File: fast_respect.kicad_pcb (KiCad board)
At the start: 2 copper layers, 70 x 110 mm, 97 parts, among them J1_1 Conn_02x04_Odd_Even, J5_1 Conn_02x03_Odd_Even, J5_2 Conn_02x03_Odd_Even, J7_1 Conn_01x02, Q2_1 IRLML6402, Q3_1 IRLML6344T, Q4_1 IRLML6344T, Q4_2 IRLML6344T, Q4_3 IRLML6344T, Q4_4 IRLML6344T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

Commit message: DRV8835のフットプリントをネットリストに反映させてPCBも更新した
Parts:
- U5_1: footprint Self-Made_Generic_Packages:WSON-12-1EP_ExpandPad_3x2mm_P0.5mm_EP1x2.65 -> DRV8835:DRV8835_ThermalExpanded_WSON-12-1EP
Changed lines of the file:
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@@
     )
   )
-  (footprint "Self-Made_Generic_Packages:WSON-12-1EP_ExpandPad_3x2mm_P0.5mm_EP1x2.65" (layer "F.Cu")
+  (footprint "DRV8835:DRV8835_ThermalExpanded_WSON-12-1EP" (layer "F.Cu")
     (at -46.435 69.39 90)
     (descr "WSON-12 http://www.ti.com/lit/ds/symlink/lm27762.pdf")
@@
         (effects (font (size 1 1) (thickness 0.15)))
     )
-    (fp_text user "${REFERENCE}" (at 0 -0.25) (layer "F.Fab")
+    (fp_text user "${REFERENCE}" (at 0 -0.25 180) (layer "F.Fab")
         (effects (font (size 0.5 0.5) (thickness 0.05)))
     )
@@
     (pad "6" smd rect (at -1.075 1.25 90) (size 0.75 0.25) (layers "F.Cu" "F.Paste" "F.Mask")
       (net 6 "GND") (pinfunction "GND") (pintype "power_in"))
+    (pad "6" smd rect (at 0 0 90) (size 1 3.975) (layers "F.Cu" "F.Mask")
+      (net 6 "GND") (pinfunction "GND") (pintype "power_in"))
     (pad "7" smd rect (at 1.075 1.25 90) (size 0.75 0.25) (layers "F.Cu" "F.Paste" "F.Mask")
       (net 7 "MOTOR2_PWM") (pinfunction "BIN2/B_ENABLE") (pintype "input"))
@@
     (pad "12" smd rect (at 1.075 -1.25 90) (size 0.75 0.25) (layers "F.Cu" "F.Paste" "F.Mask")
       (net 10 "+3.3V") (pinfunction "VCC") (pintype "power_in"))
-    (pad "13" smd rect (at 0 0 90) (size 1 3.975) (layers "F.Cu" "F.Mask"))
     (model "${KICAD6_3DMODEL_DIR}/Package_SON.3dshapes/WSON-12-1EP_3x2mm_P0.5mm_EP1x2.65.wrl"
       (offset (xyz 0 0 0))

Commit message: 距離センサのPCB位置を考慮してピン割り当てを変更した（1,2,3,4 -> 4,3,2,1）
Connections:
- U1_1 pad 10: DIST_ADC_2 -> DIST_ADC_3
- U1_1 pad 11: DIST_LED_2 -> DIST_LED_3
- U1_1 pad 20: DIST_ADC_3 -> DIST_ADC_2
- U1_1 pad 21: DIST_LED_3 -> DIST_LED_2
- U1_1 pad 22: DIST_ADC_4 -> DIST_ADC_1
- U1_1 pad 23: DIST_LED_4 -> DIST_LED_1
- U1_1 pad 8: DIST_ADC_1 -> DIST_ADC_4
- U1_1 pad 9: DIST_LED_1 -> DIST_LED_4
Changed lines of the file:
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@@
       (net 72 "NRST") (pinfunction "NRST") (pintype "input"))
     (pad "8" smd roundrect (at -5.675 -0.25 225) (size 1.55 0.3) (layers "F.Cu" "F.Paste" "F.Mask") (roundrect_rratio 0.25)
-      (net 38 "DIST_ADC_1") (pinfunction "PC0") (pintype "bidirectional"))
+      (net 35 "DIST_ADC_4") (pinfunction "PC0") (pintype "bidirectional"))
     (pad "9" smd roundrect (at -5.675 0.25 225) (size 1.55 0.3) (layers "F.Cu" "F.Paste" "F.Mask") (roundrect_rratio 0.25)
-      (net 41 "DIST_LED_1") (pinfunction "PC1") (pintype "bidirectional"))
+      (net 53 "DIST_LED_4") (pinfunction "PC1") (pintype "bidirectional"))
     (pad "10" smd roundrect (at -5.675 0.75 225) (size 1.55 0.3) (layers "F.Cu" "F.Paste" "F.Mask") (roundrect_rratio 0.25)
-      (net 37 "DIST_ADC_2") (pinfunction "PC2") (pintype "bidirectional"))
+      (net 36 "DIST_ADC_3") (pinfunction "PC2") (pintype "bidirectional"))
     (pad "11" smd roundrect (at -5.675 1.25 225) (size 1.55 0.3) (layers "F.Cu" "F.Paste" "F.Mask") (roundrect_rratio 0.25)
-      (net 45 "DIST_LED_2") (pinfunction "PC3") (pintype "bidirectional"))
+      (net 49 "DIST_LED_3") (pinfunction "PC3") (pintype "bidirectional"))
     (pad "12" smd roundrect (at -5.675 1.75 225) (size 1.55 0.3) (layers "F.Cu" "F.Paste" "F.Mask") (roundrect_rratio 0.25)
       (net 6 "GND") (pinfunction "VSSA") (pintype "power_in"))
@@
       (net 10 "+3.3V") (pinfunction "VDD") (pintype "power_in"))
     (pad "20" smd roundrect (at -2.25 5.675 225) (size 0.3 1.55) (layers "F.Cu" "F.Paste" "F.Mask") (roundrect_rratio 0.25)
-      (net 36 "DIST_ADC_3") (pinfunction "PA4") (pintype "bidirectional"))
+      (net 37 "DIST_ADC_2") (pinfunction "PA4") (pintype "bidirectional"))
     (pad "21" smd roundrect (at -1.75 5.675 225) (size 0.3 1.55) (layers "F.Cu" "F.Paste" "F.Mask") (roundrect_rratio 0.25)
-      (net 49 "DIST_LED_3") (pinfunction "PA5") (pintype "bidirectional"))
+      (net 45 "DIST_LED_2") (pinfunction "PA5") (pintype "bidirectional"))
     (pad "22" smd roundrect (at -1.25 5.675 225) (size 0.3 1.55) (layers "F.Cu" "F.Paste" "F.Mask") (roundrect_rratio 0.25)
-      (net 35 "DIST_ADC_4") (pinfunction "PA6") (pintype "bidirectional"))
+      (net 38 "DIST_ADC_1") (pinfunction "PA6") (pintype "bidirectional"))
     (pad "23" smd roundrect (at -0.75 5.675 225) (size 0.3 1.55) (layers "F.Cu" "F.Paste" "F.Mask") (roundrect_rratio 0.25)
-      (net 53 "DIST_LED_4") (pinfunction "PA7") (pintype "bidirectional"))
+      (net 41 "DIST_LED_1") (pinfunction "PA7") (pintype "bidirectional"))
     (pad "24" smd roundrect (at -0.25 5.675 225) (size 0.3 1.55) (layers "F.Cu" "F.Paste" "F.Mask") (roundrect_rratio 0.25)
       (net 39 "UI_LED_1") (pinfunction "PC4") (pintype "bidirectional"))

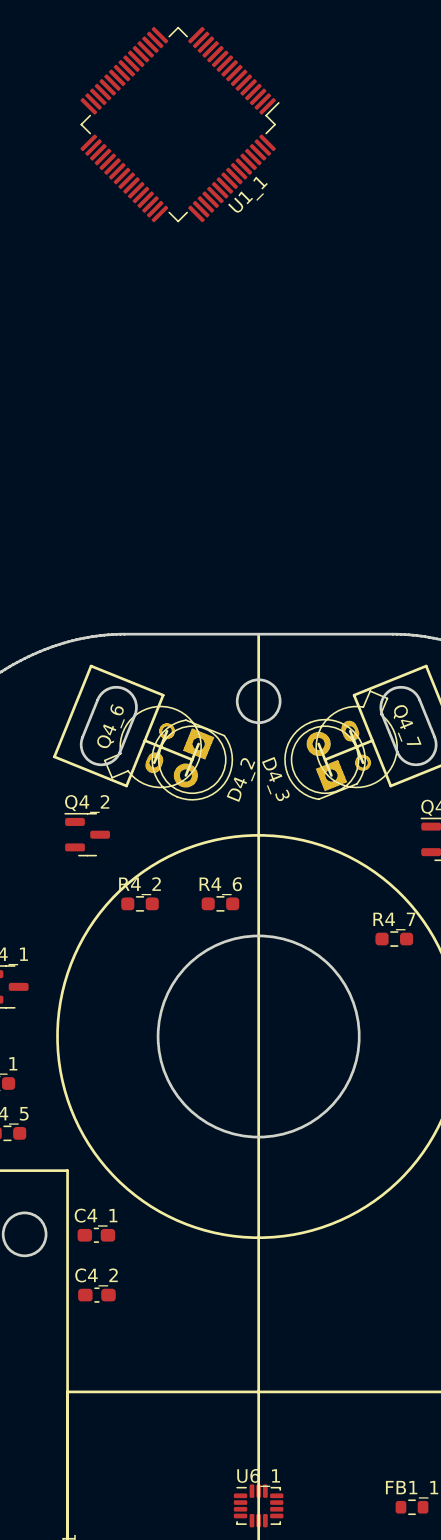
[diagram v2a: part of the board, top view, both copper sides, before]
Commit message: マイコンの位置を再調整
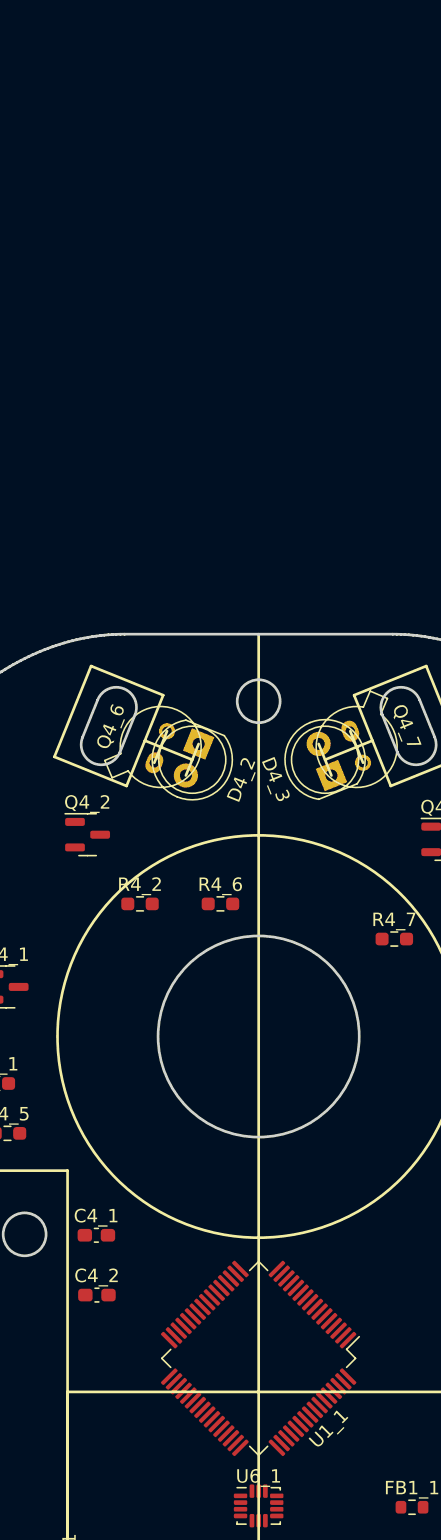
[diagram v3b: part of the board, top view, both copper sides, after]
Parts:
- moved U1_1 92.2 mm to (-35.0, 54.0)
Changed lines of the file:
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@@
   )
   (footprint "Package_QFP:LQFP-64_10x10mm_P0.5mm" (layer "F.Cu")
-    (at -41 -38 -135)
+    (at -35 54 -135)
     (descr "LQFP, 64 Pin (https://www.analog.com/media/en/technical-documentation/data-sheets/ad7606_7606-6_7606-4.pdf), generated with kicad-footprint-generator ipc_gullwing_generator.py")
     (tags "LQFP QFP")

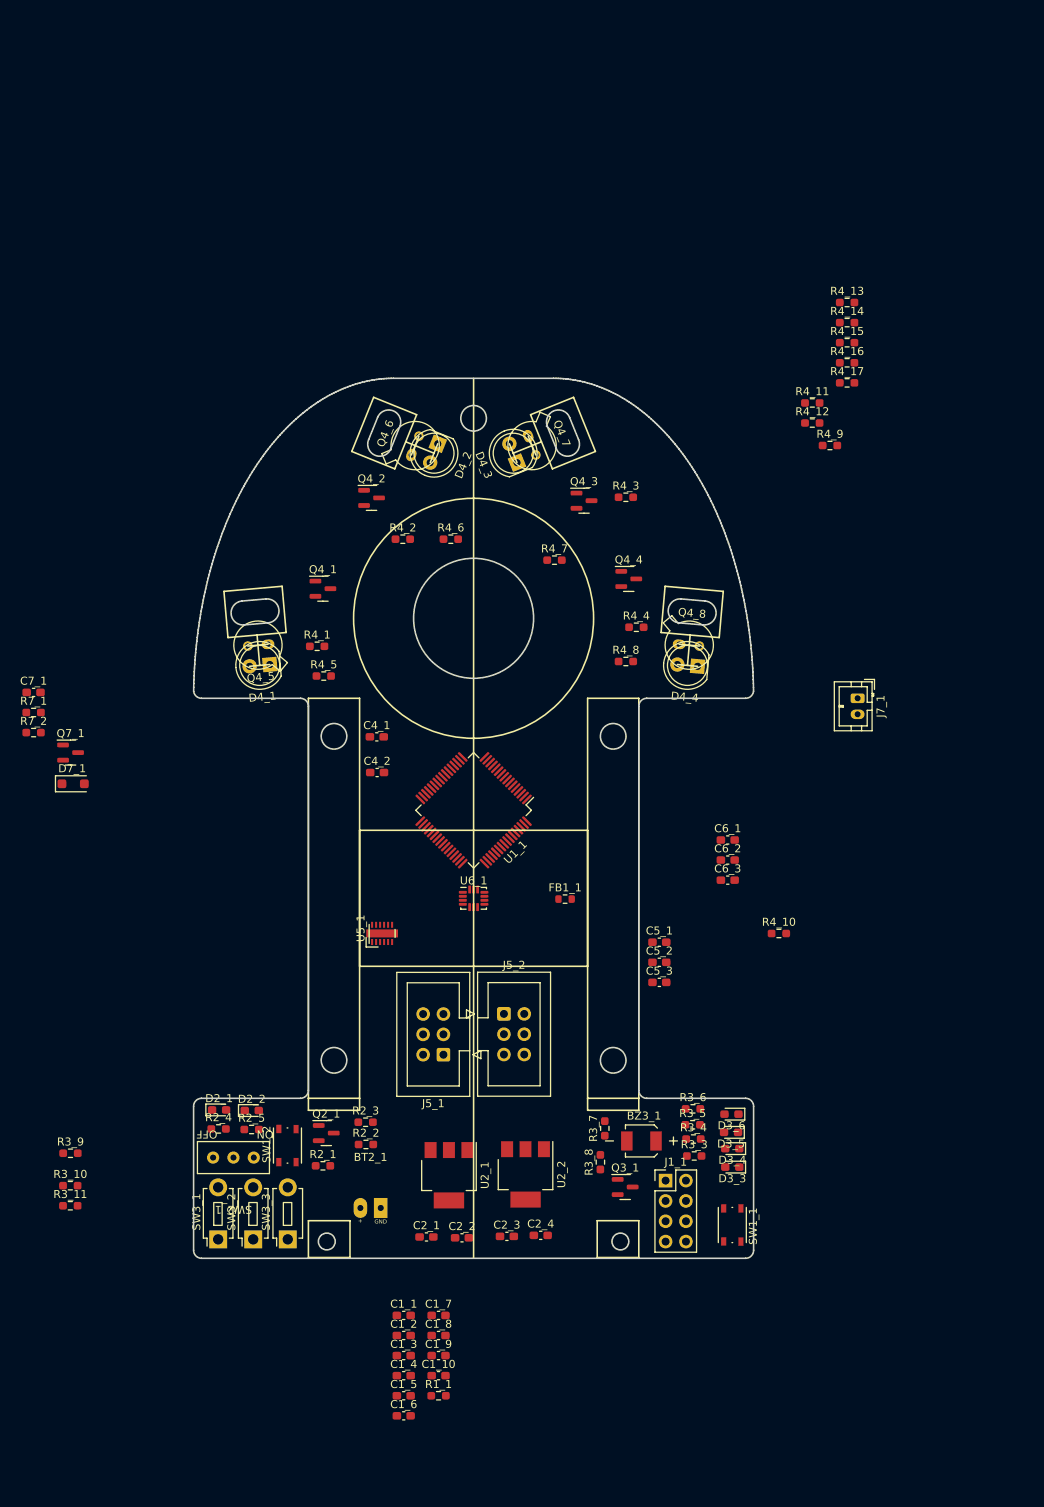
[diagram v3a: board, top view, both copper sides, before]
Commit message: UIのスイッチやLED、書き込み側や電源スイッチの配置を修正
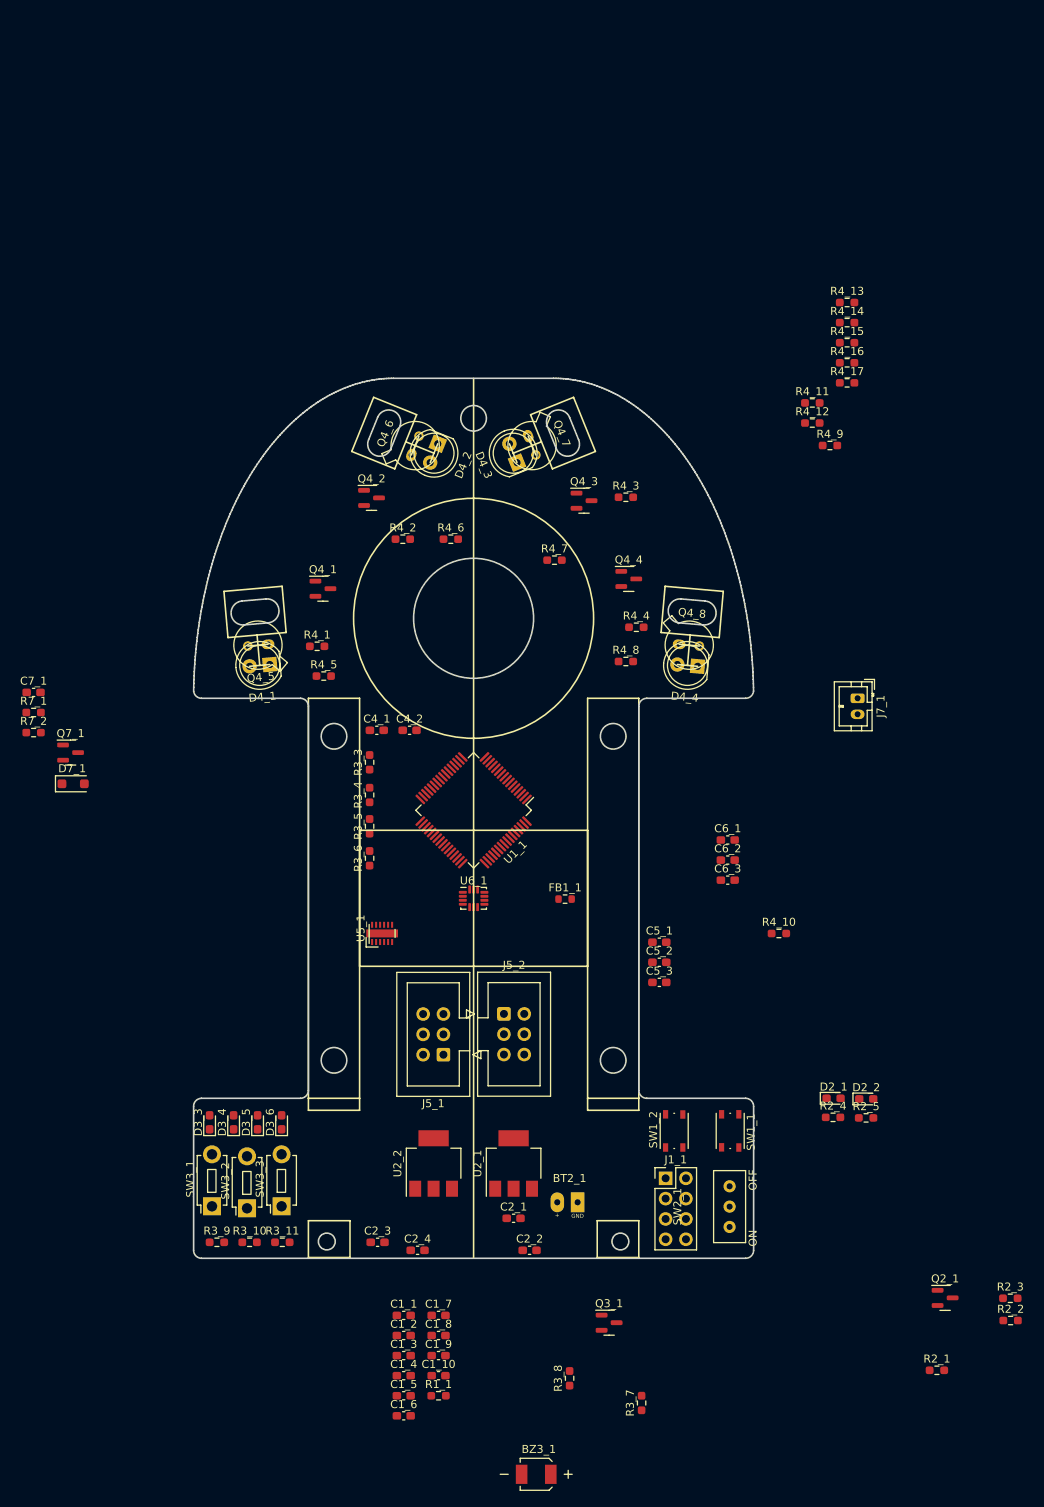
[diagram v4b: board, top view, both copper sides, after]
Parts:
- moved R2_2 83.5 mm to (32.1, 117.8)
- moved R2_3 83.5 mm to (32.1, 115.0)
- moved R2_1 80.9 mm to (22.9, 124.0)
- moved Q2_1 80.1 mm to (23.9, 115.0)
- moved D2_1 76.8 mm to (10.0, 90.0)
- moved D2_2 76.8 mm to (14.1, 90.1)
- moved R2_4 76.8 mm to (9.93, 92.4)
- moved R2_5 76.8 mm to (14.1, 92.5)
- moved D3_3 65.6 mm to (-68.0, 93.0), turned to 90 degrees
- moved R3_3 63.8 mm to (-48.0, 48.0), turned to 90 degrees
- moved D3_4 62.4 mm to (-65.0, 93.0), turned to 90 degrees
- moved SW2_1 62.3 mm to (-3.00, 103.5), turned to 90 degrees
- moved D3_5 59.2 mm to (-62.0, 93.0), turned to 90 degrees
- moved R3_4 59.1 mm to (-48.0, 52.1), turned to 90 degrees
- moved D3_6 56.2 mm to (-59.0, 93.0), turned to 90 degrees
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
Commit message: 1、２番台の簡易配置をした
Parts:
- moved C1_4 77.7 mm to (-42.9, 47.0)
- moved C1_3 77.2 mm to (-43.0, 45.0)
- moved C1_9 77.0 mm to (-22.9, 47.0)
- moved C1_6 76.6 mm to (-22.9, 56.0)
- moved C1_8 76.5 mm to (-22.9, 45.0)
- moved C1_7 75.9 mm to (-23.0, 43.0)
- moved C1_10 75.9 mm to (-45.0, 49.0), turned to 180 degrees
- moved C1_2 69.8 mm to (-23.0, 53.0)
- moved C1_5 64.2 mm to (-45.0, 63.0)
- moved R2_3 62.6 mm to (-22.9, 85.0)
- moved R2_2 62.1 mm to (-22.9, 89.0), turned to 180 degrees
- moved Q2_1 50.4 mm to (-25.9, 108.0)
- moved R2_1 47.9 mm to (-21.9, 107.0)
- moved R1_1 38.2 mm to (-16.0, 97.0)
- moved C1_1 36.2 mm to (-15.9, 94.0)
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
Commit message: 全体に全体に おおまかな部品配置完了
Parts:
- moved BZ3_1 104.3 mm to (-55.6, 36.6), turned to 90 degrees
- moved R3_7 88.2 mm to (-43.1, 44.8), turned to 0 degrees
- moved Q3_1 87.5 mm to (-51.2, 37.1)
- moved R3_8 80.1 mm to (-43.1, 47.5), turned to 0 degrees
- moved R7_2 76.5 mm to (-14.0, 36.0)
- moved R7_1 76.3 mm to (-14.1, 33.9)
- moved C7_1 76.3 mm to (-14.0, 32.2)
- moved R4_14 74.2 mm to (-52.1, 31.0)
- moved D7_1 72.4 mm to (-14.1, 38.2)
- moved Q7_1 67.7 mm to (-18.4, 36.9)
- moved R4_10 60.6 mm to (-22.6, 14.5)
- moved R4_15 55.1 mm to (-40.1, 14.5)
- moved R4_13 47.5 mm to (-18.1, 27.5)
- moved R3_3 45.0 mm to (-49.9, 93.0), turned to 0 degrees
- moved R4_16 44.9 mm to (-30.1, 14.5)
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
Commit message: 色々再配置
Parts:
- moved C5_3 24.0 mm to (-47.1, 70.5)
- moved U5_1 11.7 mm to (-35.0, 71.4), turned to 180 degrees
- moved C6_1 10.6 mm to (-41.0, 66.0), turned to 180 degrees
- moved C5_1 10.0 mm to (-22.9, 76.6)
- moved C6_3 6.48 mm to (-29.6, 63.1)
- moved C5_2 4.09 mm to (-22.9, 73.2)
- moved C1_5 3.51 mm to (-46.9, 56.3)
- moved U2_1 3.29 mm to (-32.2, 99.5)
- moved R3_6 2.34 mm to (-51.9, 99.9)
- moved U2_2 2.32 mm to (-42.7, 99.5)
- moved R3_3 2.28 mm to (-52.2, 92.8)
- moved R3_5 2.22 mm to (-52.0, 97.7)
- moved R3_4 2.16 mm to (-52.0, 95.5)
- moved C6_2 1.37 mm to (-29.7, 65.9)
- moved C2_4 1.23 mm to (-45.0, 107.2), turned to 180 degrees
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
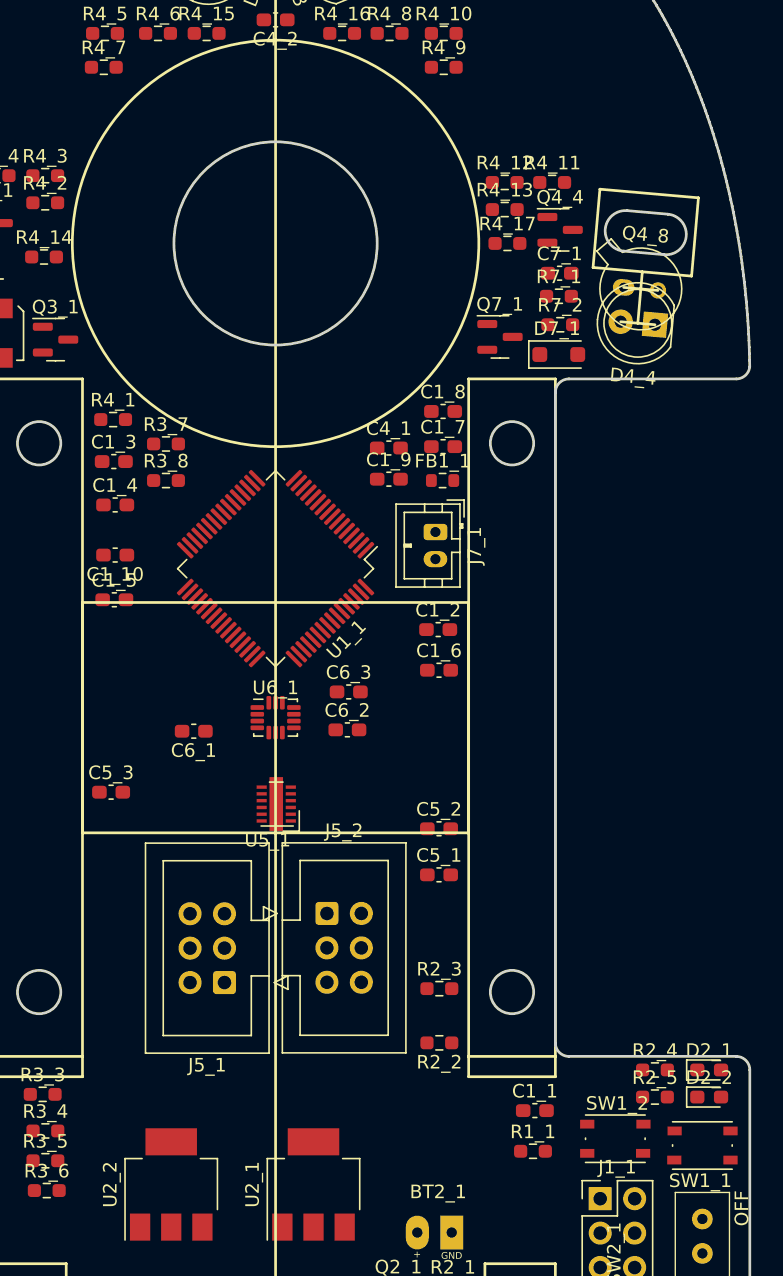
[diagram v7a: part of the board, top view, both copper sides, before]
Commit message: 吸引ファンの端子がタイヤのナットや吸引ファンマウンタに干渉しそうなので位置修正
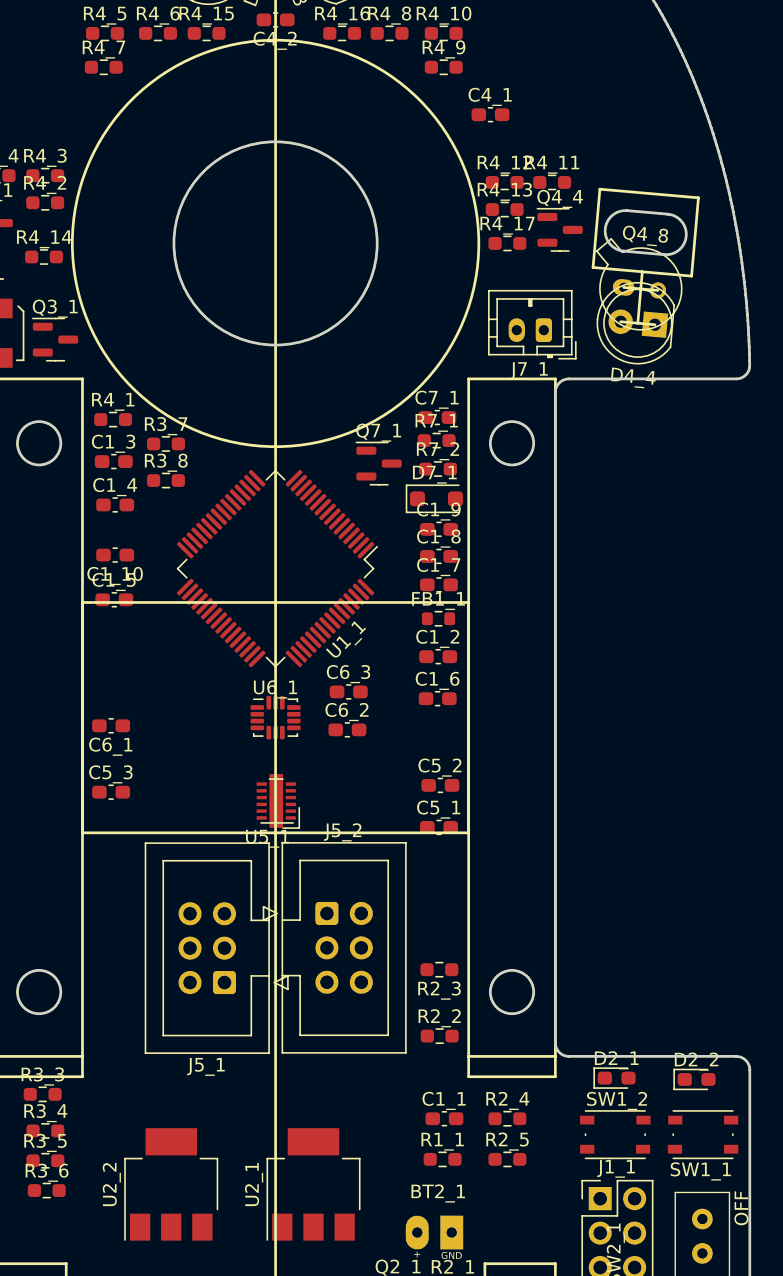
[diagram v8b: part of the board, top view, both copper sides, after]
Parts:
- moved C4_1 25.7 mm to (-19.1, 20.5)
- moved J7_1 16.9 mm to (-15.2, 36.4), turned to 180 degrees
- moved C7_1 14.0 mm to (-23.1, 42.9)
- moved D7_1 14.0 mm to (-23.1, 48.9)
- moved R7_1 14.0 mm to (-23.1, 44.5)
- moved R7_2 14.0 mm to (-23.0, 46.6)
- moved Q7_1 12.9 mm to (-27.4, 46.2)
- moved R2_5 11.8 mm to (-17.9, 97.6)
- moved R2_4 11.5 mm to (-17.9, 94.6)
- moved C1_8 10.7 mm to (-22.9, 53.1)
- moved C1_7 10.2 mm to (-22.9, 55.2)
- moved FB1_1 10.2 mm to (-23.0, 57.7)
- moved D2_1 6.85 mm to (-9.82, 91.6)
- moved C1_1 6.70 mm to (-22.5, 94.6)
- moved R1_1 6.70 mm to (-22.7, 97.6)
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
